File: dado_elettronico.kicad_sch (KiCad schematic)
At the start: 29 parts, among them Q1 2N2219, SW1 SW_DIP_x01, U1 NE555P, U2 4017

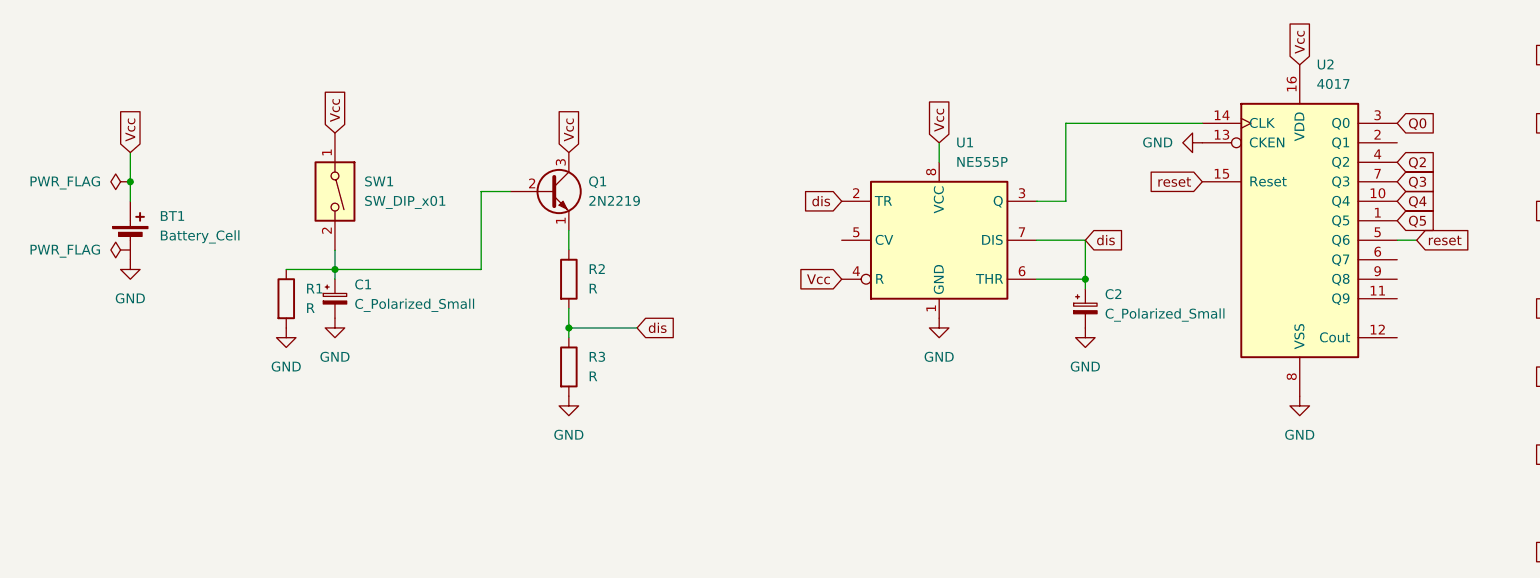
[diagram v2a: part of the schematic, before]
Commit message: schema elettrico con impronte
assegnate impronte ai componenti
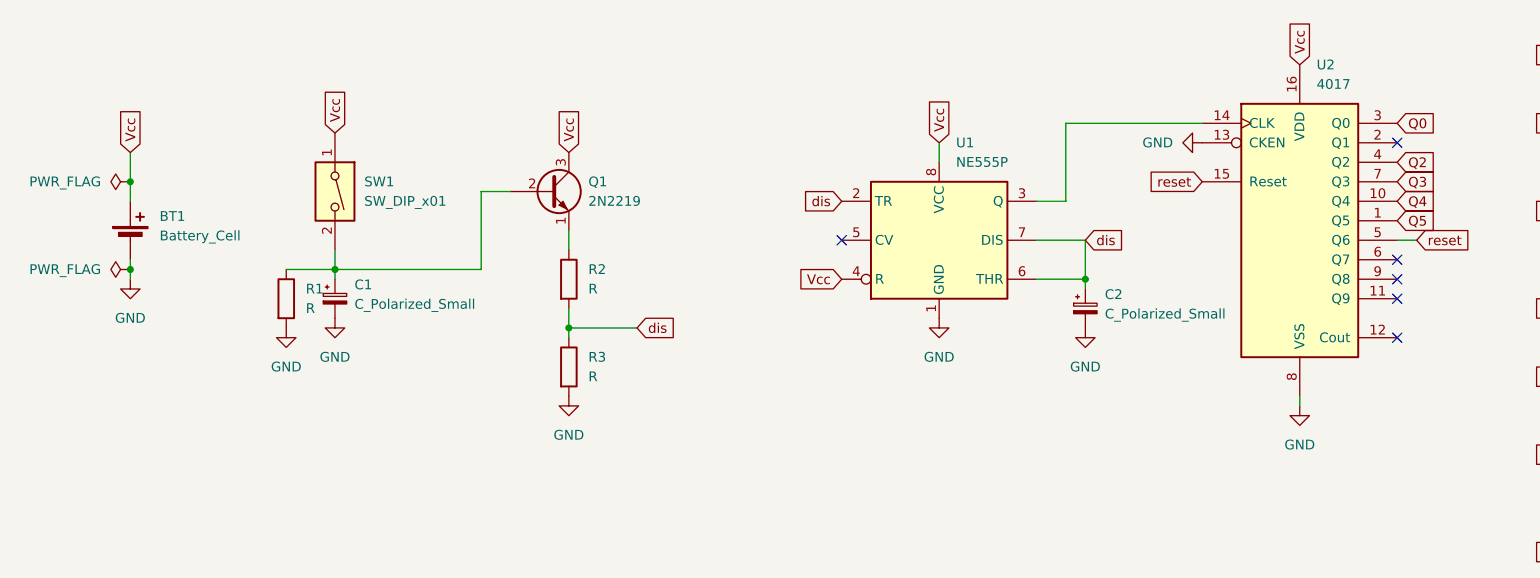
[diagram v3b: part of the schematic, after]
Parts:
- C1, C2: footprint (none) -> Capacitor_THT:CP_Radial_D5.0mm_P2.50mm
- D10, D11, D12, D13, D14, D15, D9: footprint (none) -> LED_THT:LED_D4.0mm
- R1, R2, R3, R4, R5, R6, R7: footprint (none) -> Resistor_THT:R_Axial_DIN0204_L3.6mm_D1.6mm_P5.08mm_Horizontal
- SW1: footprint (none) -> Button_Switch_THT:SW_DIP_SPSTx01_Slide_9.78x4.72mm_W7.62mm_P2.54mm
- U2: footprint (none) -> Package_DIP:DIP-16_W7.62mm_Socket
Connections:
- no-connect marks 0 -> 6
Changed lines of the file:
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@@
   (junction (at 236.22 91.44) (diameter 0) (color 0 0 0 0)
   )
+  (junction (at 27.94 86.36) (diameter 0) (color 0 0 0 0)
+  )
+  (no_connect (at 193.04 90.17))
+  (no_connect (at 193.04 85.09))
+  (no_connect (at 193.04 87.63))
+  (no_connect (at 193.04 95.25))
+  (no_connect (at 193.04 69.85))
+  (no_connect (at 120.65 82.55))
   (wire (pts (xy 149.86 67.31) (xy 149.86 77.47))
     (stroke (width 0) (type default))
@@
     (stroke (width 0) (type default))
   )
+  (wire (pts (xy 27.94 86.36) (xy 27.94 85.09))
+    (stroke (width 0) (type default))
+  )
   (wire (pts (xy 236.22 100.33) (xy 236.22 91.44))
     (stroke (width 0) (type default))
@@
   )
   (wire (pts (xy 223.52 110.49) (xy 236.22 110.49))
+    (stroke (width 0) (type default))
+  )
+  (wire (pts (xy 27.94 87.63) (xy 27.94 86.36))
+    (stroke (width 0) (type default))
+  )
+  (wire (pts (xy 180.34 104.14) (xy 180.34 102.87))
     (stroke (width 0) (type default))
   )
@@
       (effects (font (size 1.27 1.27)))
     )
-    (property "Footprint" "" (at 261.62 102.108 90)
+    (property "Footprint" "Resistor_THT:R_Axial_DIN0204_L3.6mm_D1.6mm_P5.08mm_Horizontal" (at 261.62 102.108 90)
       (effects (font (size 1.27 1.27)) hide)
     )
@@
       (effects (font (size 1.27 1.27)) (justify left))
     )
-    (property "Footprint" "" (at 54.61 90.17 0)
+    (property "Footprint" "Capacitor_THT:CP_Radial_D5.0mm_P2.50mm" (at 54.61 90.17 0)
       (effects (font (size 1.27 1.27)) hide)
     )
@@
       (effects (font (size 1.27 1.27)) (justify left))
     )
-    (property "Footprint" "" (at 152.4 91.44 0)
+    (property "Footprint" "Capacitor_THT:CP_Radial_D5.0mm_P2.50mm" (at 152.4 91.44 0)
       (effects (font (size 1.27 1.27)) hide)
     )
@@
       (effects (font (size 1.27 1.27)) (justify left))
     )
-    (property "Footprint" "" (at 54.61 76.2 0)
+    (property "Footprint" "Button_Switch_THT:SW_DIP_SPSTx01_Slide_9.78x4.72mm_W7.62mm_P2.54mm" (at 54.61 76.2 0)
       (effects (font (size 1.27 1.27)) hide)
     )
@@
       (effects (font (size 1.27 1.27)))
     )
-    (property "Footprint" "" (at 247.65 72.39 0)
+    (property "Footprint" "LED_THT:LED_D4.0mm" (at 247.65 72.39 0)
       (effects (font (size 1.27 1.27)) hide)
     )
@@
     )
   )
-  (symbol (lib_id "power:GND") (at 27.94 85.09 0) (unit 1)
-    (in_bom yes) (on_board yes) (dnp no) (fields_autoplaced)
-    (property "Reference" "#PWR05" (at 27.94 91.44 0)
-      (effects (font (size 1.27 1.27)) hide)
-    )
-    (property "Value" "GND" (at 27.94 90.17 0)
-      (effects (font (size 1.27 1.27)))
-    )
-    (property "Footprint" "" (at 27.94 85.09 0)
-      (effects (font (size 1.27 1.27)) hide)
-    )
-    (property "Datasheet" "" (at 27.94 85.09 0)
+  (symbol (lib_id "power:GND") (at 27.94 87.63 0) (unit 1)
+    (in_bom yes) (on_board yes) (dnp no) (fields_autoplaced)
+    (property "Reference" "#PWR05" (at 27.94 93.98 0)
+      (effects (font (size 1.27 1.27)) hide)
+    )
+    (property "Value" "GND" (at 27.94 92.71 0)
+      (effects (font (size 1.27 1.27)))
+    )
+    (property "Footprint" "" (at 27.94 87.63 0)
+      (effects (font (size 1.27 1.27)) hide)
+    )
+    (property "Datasheet" "" (at 27.94 87.63 0)
       (effects (font (size 1.27 1.27)) hide)
     )
@@
       (effects (font (size 1.27 1.27)))
     )
-    (property "Footprint" "" (at 247.65 114.3 0)
+    (property "Footprint" "LED_THT:LED_D4.0mm" (at 247.65 114.3 0)
       (effects (font (size 1.27 1.27)) hide)
     )
@@
       (effects (font (size 1.27 1.27)))
     )
-    (property "Footprint" "" (at 261.62 80.518 90)
+    (property "Footprint" "Resistor_THT:R_Axial_DIN0204_L3.6mm_D1.6mm_P5.08mm_Horizontal" (at 261.62 80.518 90)
       (effects (font (size 1.27 1.27)) hide)
     )
@@
       (effects (font (size 1.27 1.27)))
     )
-    (property "Footprint" "" (at 246.38 58.42 0)
+    (property "Footprint" "LED_THT:LED_D4.0mm" (at 246.38 58.42 0)
       (effects (font (size 1.27 1.27)) hide)
     )
@@
       (effects (font (size 1.27 1.27)))
     )
-    (property "Footprint" "" (at 247.65 100.33 0)
+    (property "Footprint" "LED_THT:LED_D4.0mm" (at 247.65 100.33 0)
       (effects (font (size 1.27 1.27)) hide)
     )
@@
       (effects (font (size 1.27 1.27)))
     )
-    (property "Footprint" "" (at 247.65 91.44 0)
+    (property "Footprint" "LED_THT:LED_D4.0mm" (at 247.65 91.44 0)
       (effects (font (size 1.27 1.27)) hide)
     )
@@
     )
   )
-  (symbol (lib_id "power:PWR_FLAG") (at 27.94 83.82 90) (unit 1)
-    (in_bom yes) (on_board yes) (dnp no) (fields_autoplaced)
-    (property "Reference" "#FLG02" (at 26.035 83.82 0)
-      (effects (font (size 1.27 1.27)) hide)
-    )
-    (property "Value" "PWR_FLAG" (at 24.13 83.82 90)
-      (effects (font (size 1.27 1.27)) (justify left))
-    )
-    (property "Footprint" "" (at 27.94 83.82 0)
-      (effects (font (size 1.27 1.27)) hide)
-    )
-    (property "Datasheet" "~" (at 27.94 83.82 0)
+  (symbol (lib_id "power:PWR_FLAG") (at 27.94 86.36 90) (unit 1)
+    (in_bom yes) (on_board yes) (dnp no) (fields_autoplaced)
+    (property "Reference" "#FLG02" (at 26.035 86.36 0)
+      (effects (font (size 1.27 1.27)) hide)
+    )
+    (property "Value" "PWR_FLAG" (at 24.13 86.36 90)
+      (effects (font (size 1.27 1.27)) (justify left))
+    )
+    (property "Footprint" "" (at 27.94 86.36 0)
+      (effects (font (size 1.27 1.27)) hide)
+    )
+    (property "Datasheet" "~" (at 27.94 86.36 0)
       (effects (font (size 1.27 1.27)) hide)
     )
@@
       (effects (font (size 1.27 1.27)))
     )
-    (property "Footprint" "" (at 248.92 123.19 0)
+    (property "Footprint" "LED_THT:LED_D4.0mm" (at 248.92 123.19 0)
       (effects (font (size 1.27 1.27)) hide)
     )
@@
       (effects (font (size 1.27 1.27)))
     )
-    (property "Footprint" "" (at 260.35 60.198 90)
+    (property "Footprint" "Resistor_THT:R_Axial_DIN0204_L3.6mm_D1.6mm_P5.08mm_Horizontal" (at 260.35 60.198 90)
       (effects (font (size 1.27 1.27)) hide)
     )
@@
       (effects (font (size 1.27 1.27)) (justify left))
     )
-    (property "Footprint" "" (at 180.34 80.01 0)
+    (property "Footprint" "Package_DIP:DIP-16_W7.62mm_Socket" (at 180.34 80.01 0)
       (effects (font (size 1.27 1.27)) hide)
     )
@@
       (effects (font (size 1.27 1.27)) (justify left))
     )
-    (property "Footprint" "" (at 46.482 90.17 90)
+    (property "Footprint" "Resistor_THT:R_Axial_DIN0204_L3.6mm_D1.6mm_P5.08mm_Horizontal" (at 46.482 90.17 90)
       (effects (font (size 1.27 1.27)) hide)
     )
@@
     )
   )
-  (symbol (lib_id "power:GND") (at 180.34 102.87 0) (unit 1)
-    (in_bom yes) (on_board yes) (dnp no) (fields_autoplaced)
-    (property "Reference" "#PWR01" (at 180.34 109.22 0)
-      (effects (font (size 1.27 1.27)) hide)
-    )
-    (property "Value" "GND" (at 180.34 107.95 0)
-      (effects (font (size 1.27 1.27)))
-    )
-    (property "Footprint" "" (at 180.34 102.87 0)
-      (effects (font (size 1.27 1.27)) hide)
-    )
-    (property "Datasheet" "" (at 180.34 102.87 0)
+  (symbol (lib_id "power:GND") (at 180.34 104.14 0) (unit 1)
+    (in_bom yes) (on_board yes) (dnp no) (fields_autoplaced)
+    (property "Reference" "#PWR01" (at 180.34 110.49 0)
+      (effects (font (size 1.27 1.27)) hide)
+    )
+    (property "Value" "GND" (at 180.34 109.22 0)
+      (effects (font (size 1.27 1.27)))
+    )
+    (property "Footprint" "" (at 180.34 104.14 0)
+      (effects (font (size 1.27 1.27)) hide)
+    )
+    (property "Datasheet" "" (at 180.34 104.14 0)
       (effects (font (size 1.27 1.27)) hide)
     )
@@
       (effects (font (size 1.27 1.27)) (justify left))
     )
-    (property "Footprint" "" (at 83.312 99.06 90)
+    (property "Footprint" "Resistor_THT:R_Axial_DIN0204_L3.6mm_D1.6mm_P5.08mm_Horizontal" (at 83.312 99.06 90)
       (effects (font (size 1.27 1.27)) hide)
     )
@@
       (effects (font (size 1.27 1.27)))
     )
-    (property "Footprint" "" (at 247.65 78.74 0)
+    (property "Footprint" "LED_THT:LED_D4.0mm" (at 247.65 78.74 0)
       (effects (font (size 1.27 1.27)) hide)
     )
@@
       (effects (font (size 1.27 1.27)) (justify left))
     )
-    (property "Footprint" "" (at 83.312 87.63 90)
+    (property "Footprint" "Resistor_THT:R_Axial_DIN0204_L3.6mm_D1.6mm_P5.08mm_Horizontal" (at 83.312 87.63 90)
       (effects (font (size 1.27 1.27)) hide)
     )
@@
       (effects (font (size 1.27 1.27)))
     )
-    (property "Footprint" "" (at 261.62 124.968 90)
-      (effects (font (size 1.27 1.27)) hide)
-    )
+    (property "Footprint" "Resistor_THT:R_Axial_DIN0204_L3.6mm_D1.6mm_P5.08mm_Horizontal" (at 261.62 124.968 90)
+      (effects (font (size 1.27 1.27)) hide)
+    )

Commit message: aggiunta impronta transistor e posizionato componenti
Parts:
- Q1: footprint Package_TO_SOT_THT:TO-39-3 -> Library:TO92_S9014_127P510H650-3
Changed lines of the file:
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@@
       (effects (font (size 1.27 1.27)) (justify left))
     )
-    (property "Footprint" "Package_TO_SOT_THT:TO-39-3" (at 87.63 78.105 0)
+    (property "Footprint" "Library:TO92_S9014_127P510H650-3" (at 87.63 78.105 0)
       (effects (font (size 1.27 1.27) italic) (justify left) hide)
     )
